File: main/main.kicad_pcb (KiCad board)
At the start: 2 copper layers, 31.2 x 57.3 mm, 24 parts, among them IC1 MB1010-000, M1 Motor_DC, P1 Digital, P2 Analog, P3 CONN_01X01, P4 CONN_01X01, P5 CONN_01X01, P6 CONN_01X01, Q1 PN2222A, U1 SW_PWR_BTN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

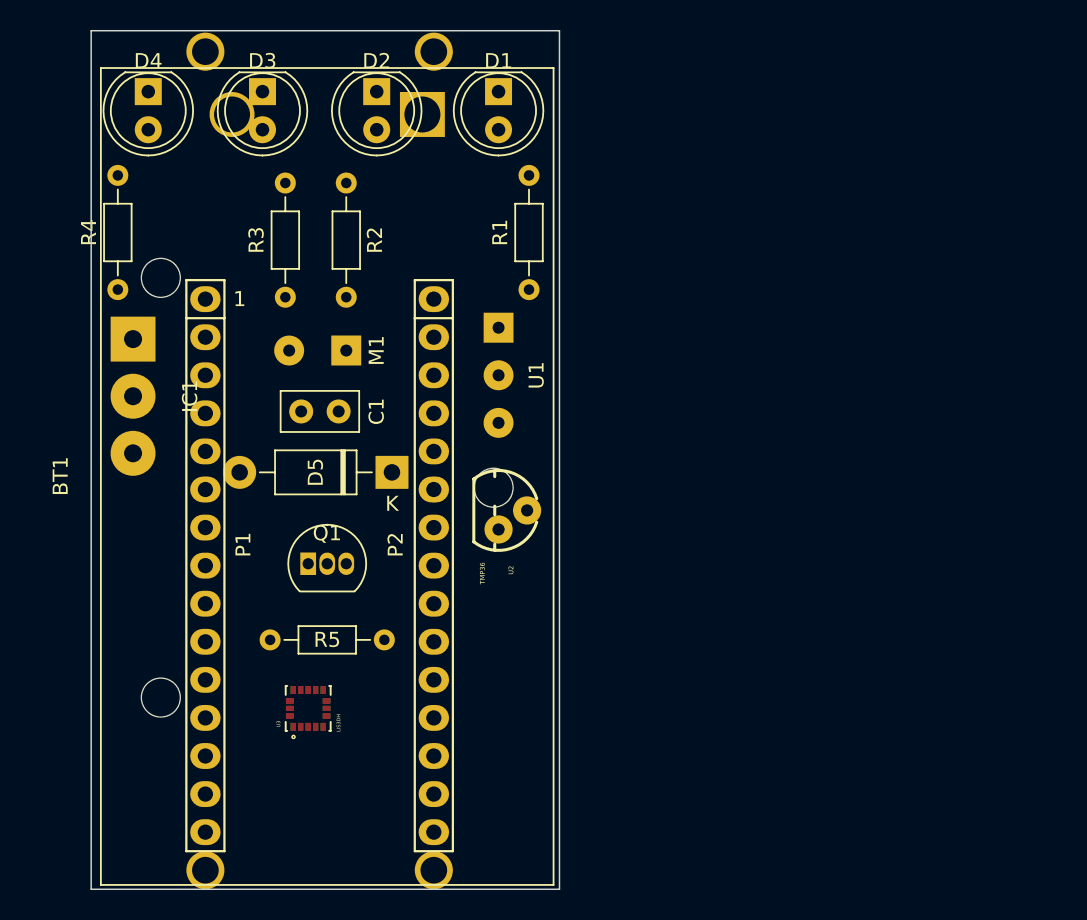
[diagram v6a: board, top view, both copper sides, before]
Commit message: pcb: Fixed Power button wirepad footprint
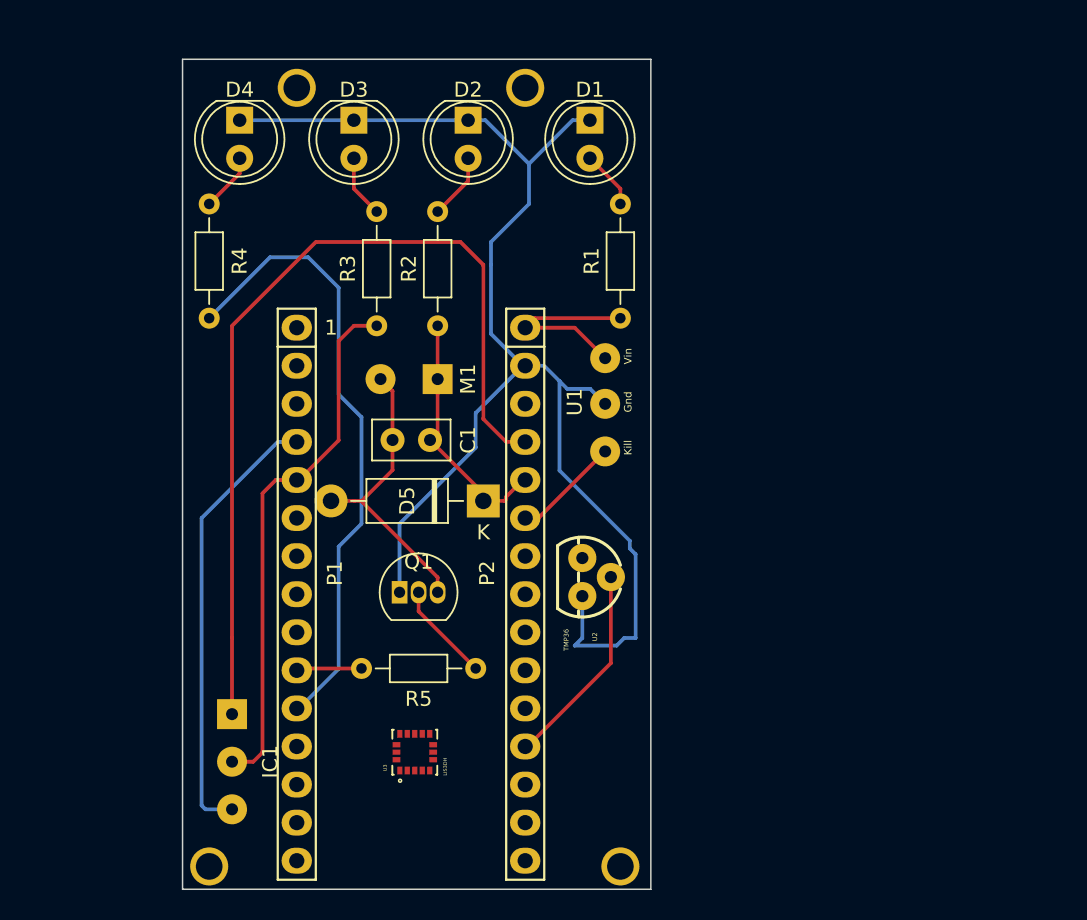
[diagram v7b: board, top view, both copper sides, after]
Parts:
- removed BT1: Battery, Battery:BatteryHolder_Eagle_12BH611-GR
- IC1: footprint Connector_Wire:SolderWirePad_1x03_P3.81mm_Drill1.2mm -> MB1010:SolderWirePad_1x03_P3.175mm_Drill0.8mm
- U1: footprint Connector_Wire:SolderWirePad_1x03_P3.175mm_Drill0.8mm -> 1400:SolderWirePad_3holes_1x03_P3.175mm_Drill0.8mm
- U3: footprint PQFN50P300X300X100-16N -> LIS3DH:PQFN50P300X300X100-16N
- moved IC1 25.9 mm to (141.2, 98.9)
- moved P5 12.4 mm to (167.1, 109.1)
- moved R2 11.3 mm to (154.9, 73.0), turned to 90 degrees
- moved U3 7.69 mm to (153.4, 101.5)
- moved U1 7.36 mm to (166.1, 75.1)
- moved U2 7.14 mm to (164.6, 89.8)
- moved P3 6.56 mm to (145.5, 57.1)
- moved P6 6.56 mm to (160.8, 57.1)
- moved D5 6.39 mm to (158.0, 84.7)
- moved M1 6.39 mm to (154.9, 76.6)
- moved P1 6.39 mm to (145.5, 73.2)
- moved P2 6.39 mm to (160.8, 73.2)
- moved Q1 6.39 mm to (152.4, 90.8)
- moved R1 6.39 mm to (167.1, 72.5)
- moved R3 6.39 mm to (150.9, 73.0)
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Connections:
- U1 pad 2: Net-(U1-Pad2) -> /Vin
- U1 pad 3: Net-(U1-Pad3) -> GND
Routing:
- net GND: track 0.00 -> 123.0 mm
- net +5V: track 0.00 -> 59.3 mm
- net /8: track 0.00 -> 41.7 mm
- net /2: track 0.00 -> 35.9 mm
- net Net-(C1-Pad2): track 0.00 -> 19.6 mm
- net /A7: track 0.00 -> 16.8 mm
- net /A0: track 0.00 -> 13.8 mm
- net /Vin: track 0.00 -> 12.9 mm
- net /A6: track 0.00 -> 7.18 mm
- net Net-(Q1-Pad2): track 0.00 -> 6.66 mm
- net Net-(D2-Pad2): track 0.00 -> 4.40 mm
- net /7: track 0.00 -> 4.37 mm
- net Net-(D3-Pad2): track 0.00 -> 4.19 mm
- net Net-(D4-Pad2): track 0.00 -> 3.89 mm
- net Net-(D1-Pad2): track 0.00 -> 3.89 mm
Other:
- board size 31.2 x 57.3 mm -> 31.2 x 55.4 mm

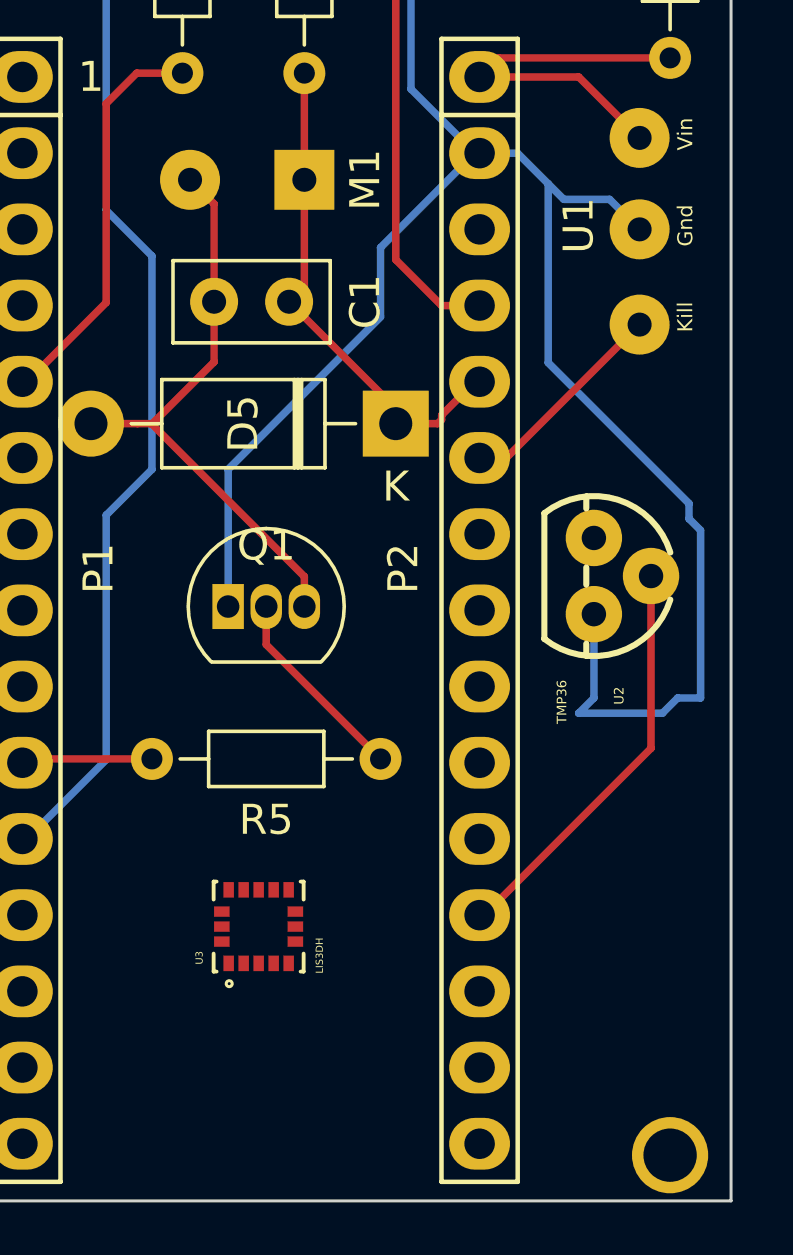
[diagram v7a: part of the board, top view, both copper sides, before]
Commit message: pcb: Corrected accelerometer I2C wirepad connections
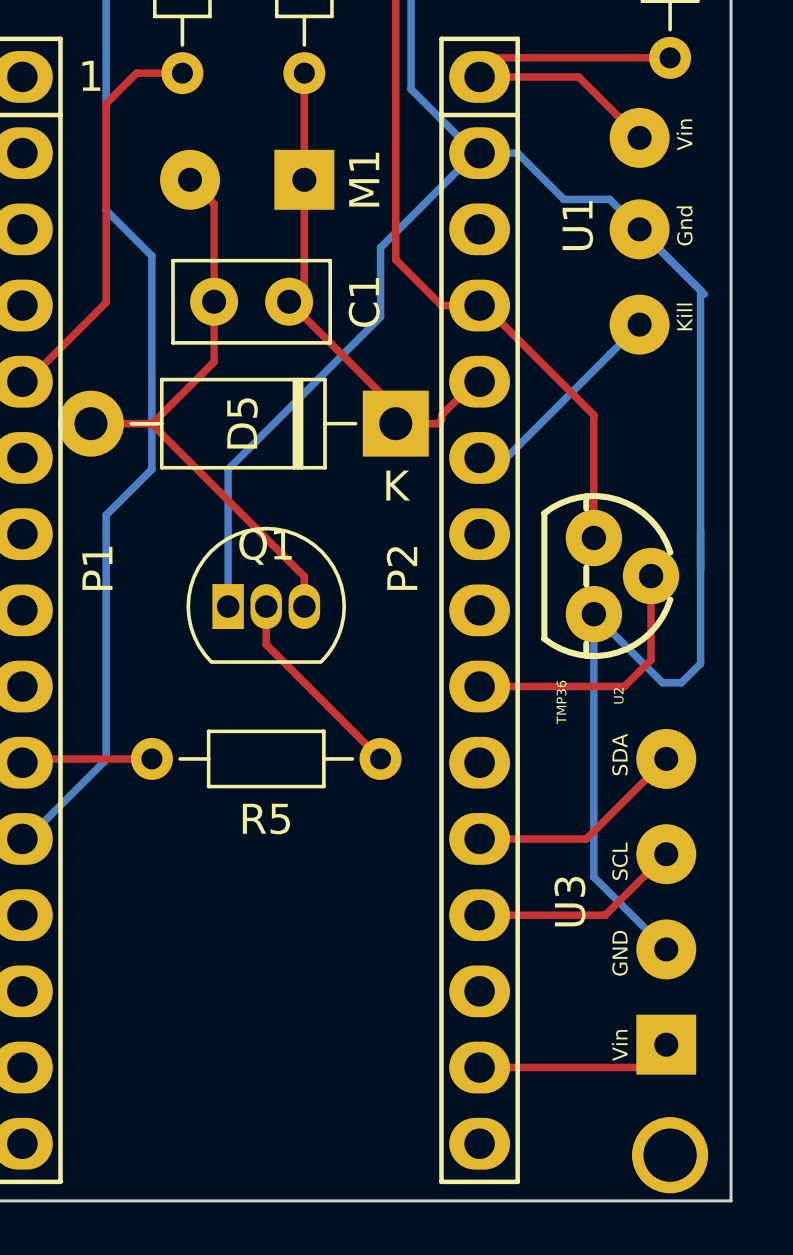
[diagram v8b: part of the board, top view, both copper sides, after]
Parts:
- U3: footprint LIS3DH:PQFN50P300X300X100-16N -> 1400:SolderWirePad_1x04_P3.175mm_Drill0.8mm_LIS3DH_I2C
- moved U3 14.1 mm to (167.0, 105.4)
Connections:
- U2 pad 2: /A0 -> /A3
- U3 pad 14: +5V -> +3V3
- U3 pad 4: /A5 -> /A1
- U3 pad 6: /A4 -> /A0
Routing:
- net GND: track 123.0 -> 132.6 mm
- net +5V: track 59.3 -> 68.7 mm
- net /A3: track 0.00 -> 8.88 mm
- net /A1: track 0.00 -> 7.33 mm
- net /A0: track 13.8 -> 7.22 mm
- net +3V3: track 0.00 -> 6.54 mm
- net /A6: track 7.18 -> 8.06 mm
